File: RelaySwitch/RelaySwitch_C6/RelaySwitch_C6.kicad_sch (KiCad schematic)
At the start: 46 parts, among them J1 AC_MAINS_IN, J3 LOAD_CH1, J4 LOAD_CH2, J5 SW1_INPUT, J6 SW2_INPUT, K1 G5Q-1-DC5, K2 G5Q-1-DC5, Q1 MMBT8050, Q2 MMBT8050, U1 HLK-2M05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

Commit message: relay after layout design
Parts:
- F1: value T250mA/250V -> Littelfuse 443.500; footprint Fuse:Fuseholder_Clip-5x20mm_Littelfuse_111_Inline_P20.00x5.00mm_D1.05mm_Horizontal -> easyeda2kicad:0443500DR; symbol Device:Fuse_Small -> 0443_500:0443.500; Height (none) -> 3.05; Manufacturer_Name (none) -> LITTELFUSE; Manufacturer_Part_Number (none) -> 0443.500
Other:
- moved on the sheet: RV1
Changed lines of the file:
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@@
 	)
 	(junction
+		(at 55.88 25.4)
+		(diameter 0)
+		(color 0 0 0 0)
+	)
+	(junction
 		(at 30.48 163.83)
 		(diameter 0)
@@
 	)
 	(junction
+		(at 49.53 39.37)
+		(diameter 0)
+		(color 0 0 0 0)
+	)
+	(junction
 		(at 90.17 88.9)
 		(diameter 0)
@@
 	)
 	(junction
-		(at 49.53 39.37)
-		(diameter 0)
-		(color 0 0 0 0)
-	)
-	(junction
 		(at 77.47 86.36)
 		(diameter 0)
@@
 	(wire
 		(pts
-			(xy 55.88 36.83) (xy 55.88 40.64)
-		)
-		(stroke
-			(width 0)
-			(type default)
-		)
-	)
-	(wire
-		(pts
 			(xy 30.48 157.48) (xy 30.48 163.83)
 		)
@@
 	(wire
 		(pts
-			(xy 30.48 36.83) (xy 44.45 36.83)
-		)
-		(stroke
-			(width 0)
-			(type default)
-		)
-	)
-	(wire
-		(pts
 			(xy 215.9 102.87) (xy 215.9 105.41)
 		)
@@
 	(wire
 		(pts
-			(xy 55.88 49.53) (xy 55.88 48.26)
-		)
-		(stroke
-			(width 0)
-			(type default)
-		)
-	)
-	(wire
-		(pts
 			(xy 262.89 46.99) (xy 265.43 46.99)
 		)
@@
 	(wire
 		(pts
+			(xy 30.48 36.83) (xy 31.75 36.83)
+		)
+		(stroke
+			(width 0)
+			(type default)
+		)
+	)
+	(wire
+		(pts
 			(xy 156.21 132.08) (xy 156.21 142.24)
 		)
@@
 	(wire
 		(pts
-			(xy 49.53 39.37) (xy 58.42 39.37)
+			(xy 30.48 39.37) (xy 49.53 39.37)
 		)
 		(stroke
@@
 	(wire
 		(pts
+			(xy 55.88 25.4) (xy 55.88 36.83)
+		)
+		(stroke
+			(width 0)
+			(type default)
+		)
+	)
+	(wire
+		(pts
 			(xy 224.79 58.42) (xy 222.25 58.42)
 		)
@@
 	(wire
 		(pts
+			(xy 49.53 25.4) (xy 55.88 25.4)
+		)
+		(stroke
+			(width 0)
+			(type default)
+		)
+	)
+	(wire
+		(pts
 			(xy 106.68 165.1) (xy 125.73 165.1)
 		)
@@
 	(wire
 		(pts
-			(xy 30.48 123.19) (xy 30.48 127)
+			(xy 49.53 39.37) (xy 58.42 39.37)
 		)
 		(stroke
@@
 	(wire
 		(pts
-			(xy 222.25 58.42) (xy 222.25 76.2)
+			(xy 30.48 123.19) (xy 30.48 127)
 		)
 		(stroke
@@
 	(wire
 		(pts
-			(xy 129.54 130.81) (xy 125.73 130.81)
+			(xy 222.25 58.42) (xy 222.25 76.2)
 		)
 		(stroke
@@
 	(wire
 		(pts
-			(xy 262.89 38.1) (xy 267.97 38.1)
+			(xy 129.54 130.81) (xy 125.73 130.81)
 		)
 		(stroke
@@
 	(wire
 		(pts
-			(xy 77.47 63.5) (xy 83.82 63.5)
+			(xy 262.89 38.1) (xy 267.97 38.1)
 		)
 		(stroke
@@
 	(wire
 		(pts
-			(xy 30.48 163.83) (xy 43.18 163.83)
+			(xy 77.47 63.5) (xy 83.82 63.5)
 		)
 		(stroke
@@
 	(wire
 		(pts
-			(xy 49.53 39.37) (xy 49.53 49.53)
+			(xy 30.48 163.83) (xy 43.18 163.83)
 		)
 		(stroke
@@
 	(wire
 		(pts
-			(xy 55.88 36.83) (xy 55.88 25.4)
-		)
-		(stroke
-			(width 0)
-			(type default)
-		)
-	)
-	(wire
-		(pts
 			(xy 68.58 165.1) (xy 106.68 165.1)
 		)
@@
 	(wire
 		(pts
-			(xy 30.48 39.37) (xy 49.53 39.37)
-		)
-		(stroke
-			(width 0)
-			(type default)
-		)
-	)
-	(wire
-		(pts
 			(xy 267.97 38.1) (xy 273.05 38.1)
 		)
@@
 	(wire
 		(pts
-			(xy 49.53 49.53) (xy 55.88 49.53)
-		)
-		(stroke
-			(width 0)
-			(type default)
-		)
-	)
-	(wire
-		(pts
 			(xy 175.26 151.13) (xy 175.26 157.48)
 		)
@@
 	(wire
 		(pts
+			(xy 49.53 34.29) (xy 49.53 39.37)
+		)
+		(stroke
+			(width 0)
+			(type default)
+		)
+	)
+	(wire
+		(pts
 			(xy 30.48 41.91) (xy 44.45 41.91)
 		)
@@
 	(wire
 		(pts
+			(xy 49.53 26.67) (xy 49.53 25.4)
+		)
+		(stroke
+			(width 0)
+			(type default)
+		)
+	)
+	(wire
+		(pts
 			(xy 83.82 60.96) (xy 83.82 63.5)
 		)
@@
 	)
 	(label "L"
-		(at 34.29 36.83 0)
+		(at 30.48 36.83 0)
 		(effects
 			(font
@@
 	(symbol
 		(lib_id "Device:Varistor")
-		(at 55.88 44.45 0)
+		(at 49.53 30.48 0)
 		(unit 1)
 		(exclude_from_sim no)
@@
 		(dnp no)
 		(property "Reference" "RV1"
-			(at 51.054 44.958 0)
+			(at 50.8 29.972 0)
 			(effects
 				(font
@@
 		)
 		(property "Value" "275VAC MOV"
-			(at 56.134 49.276 0)
+			(at 36.83 26.924 0)
 			(effects
 				(font
@@
 		)
 		(property "Footprint" "Varistor:RV_Disc_D7mm_W3.4mm_P5mm"
-			(at 54.102 44.45 90)
+			(at 47.752 30.48 90)
 			(effects
 				(font
@@
 		)
 		(property "Datasheet" "~"
-			(at 55.88 44.45 0)
+			(at 49.53 30.48 0)
 			(effects
 				(font
@@
 		)
 		(property "Description" "Voltage dependent resistor"
-			(at 55.88 44.45 0)
+			(at 49.53 30.48 0)
 			(effects
 				(font
@@
 		)
 		(property "Sim.Name" "kicad_builtin_varistor"
-			(at 55.88 44.45 0)
+			(at 49.53 30.48 0)
 			(effects
 				(font
@@
 		)
 		(property "Sim.Device" "SUBCKT"
-			(at 55.88 44.45 0)
+			(at 49.53 30.48 0)
 			(effects
 				(font
@@
 		)
 		(property "Sim.Pins" "1=A 2=B"
-			(at 55.88 44.45 0)
+			(at 49.53 30.48 0)
 			(effects
 				(font
@@
 		)
 		(property "Sim.Params" "threshold=1k"
-			(at 55.88 44.45 0)
+			(at 49.53 30.48 0)
 			(effects
 				(font
@@
 		)
 		(property "Sim.Library" "${KICAD9_SYMBOL_DIR}/Simulation_SPICE.sp"
-			(at 55.88 44.45 0)
+			(at 49.53 30.48 0)
 			(effects
 				(font
@@
 	)
 	(symbol
-		(lib_id "Device:Fuse_Small")
-		(at 46.99 36.83 0)
+		(lib_id "0443_500:0443.500")
+		(at 31.75 36.83 0)
 		(unit 1)
 		(exclude_from_sim no)
@@
 		(dnp no)
 		(property "Reference" "F1"
-			(at 46.736 34.798 0)
+			(at 40.64 34.544 0)
 			(effects
 				(font
@@
 			)
 		)
-		(property "Value" "T250mA/250V"
-			(at 46.228 31.75 0)
+		(property "Value" "Littelfuse 443.500"
+			(at 36.576 32.766 0)
 			(effects
 				(font
@@
 			)
 		)
-		(property "Footprint" "Fuse:Fuseholder_Clip-5x20mm_Littelfuse_111_Inline_P20.00x5.00mm_D1.05mm_Horizontal"
-			(at 46.99 36.83 0)
+		(property "Footprint" "easyeda2kicad:0443500DR"
+			(at 45.72 133.02 0)
 			(effects
 				(font
 					(size 1.27 1.27)
 				)
+				(justify left top)
 				(hide yes)
 			)
 		)
-		(property "Datasheet" ""
-			(at 46.99 36.83 0)
+		(property "Datasheet" "https://www.littelfuse.com/~/media/electronics/datasheets/fuses/littelfuse_fuse_443_datasheet.pdf.pdf"
+			(at 45.72 233.02 0)
 			(effects
 				(font
 					(size 1.27 1.27)
 				)
+				(justify left top)
 				(hide yes)
 			)
 		)
-		(property "Description" ""
-			(at 46.99 36.83 0)
+		(property "Description" "Surface Mount Fuses 280VAC 0.5A .6ohms 443LC NANO2"
+			(at 31.75 36.83 0)
+			(effects
+				(font
+					(size 1.27 1.27)
+				)
+				(hide yes)
+			)
+		)
+		(property "Height" "3.05"
+			(at 45.72 433.02 0)
+			(effects
+				(font
+					(size 1.27 1.27)
+				)
+				(justify left top)
+				(hide yes)
+			)
+		)
+		(property "Manufacturer_Name" "LITTELFUSE"
+			(at 45.72 533.02 0)
 			(effects
 				(font
 					(size 1.27 1.27)
 				)
+				(justify left top)
+				(hide yes)
+			)
+		)
+		(property "Manufacturer_Part_Number" "0443.500"
+			(at 45.72 633.02 0)
+			(effects
+				(font
+					(size 1.27 1.27)
+				)
+				(justify left top)
+				(hide yes)
+			)
+		)
+		(property "Mouser Part Number" ""
+			(at 45.72 733.02 0)
+			(effects
+				(font
+					(size 1.27 1.27)
+				)
+				(justify left top)
+				(hide yes)
+			)
+		)
+		(property "Mouser Price/Stock" ""
+			(at 45.72 833.02 0)
+			(effects
+				(font
+					(size 1.27 1.27)
+				)
+				(justify left top)
+				(hide yes)
+			)
+		)
+		(property "Arrow Part Number" ""
+			(at 45.72 933.02 0)
+			(effects
+				(font
+					(size 1.27 1.27)
+				)
+				(justify left top)
+				(hide yes)
+			)
+		)
+		(property "Arrow Price/Stock" ""
+			(at 45.72 1033.02 0)
+			(effects
+				(font
+					(size 1.27 1.27)
+				)
+				(justify left top)
 				(hide yes)
 			)

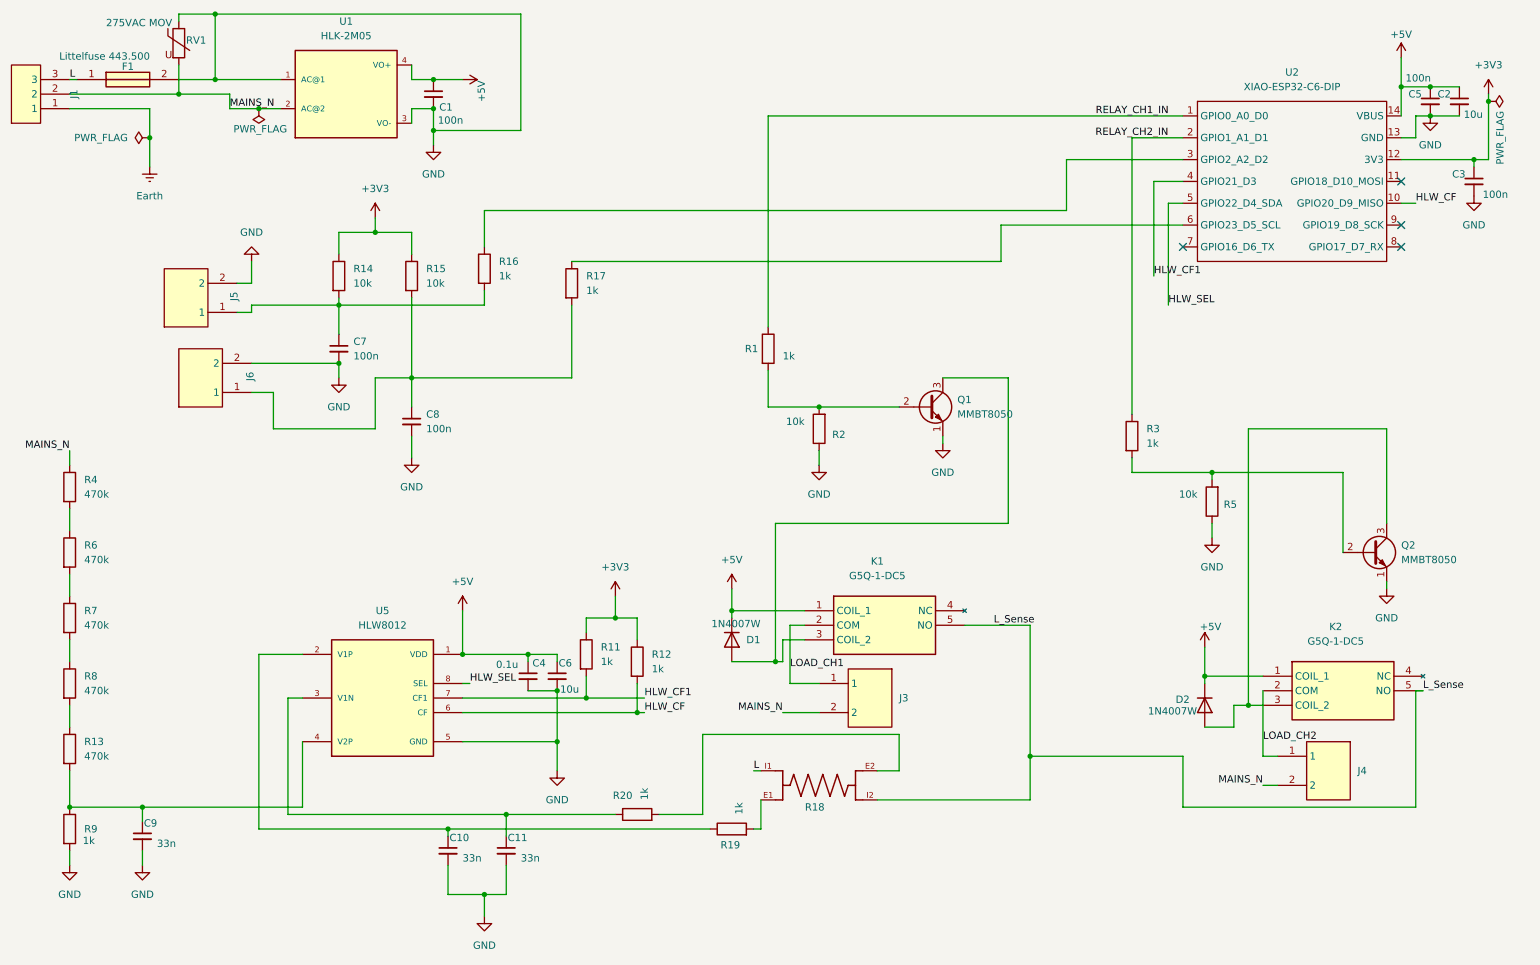
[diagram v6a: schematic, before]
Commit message: replaced the Q1 and 2 with Dual driver
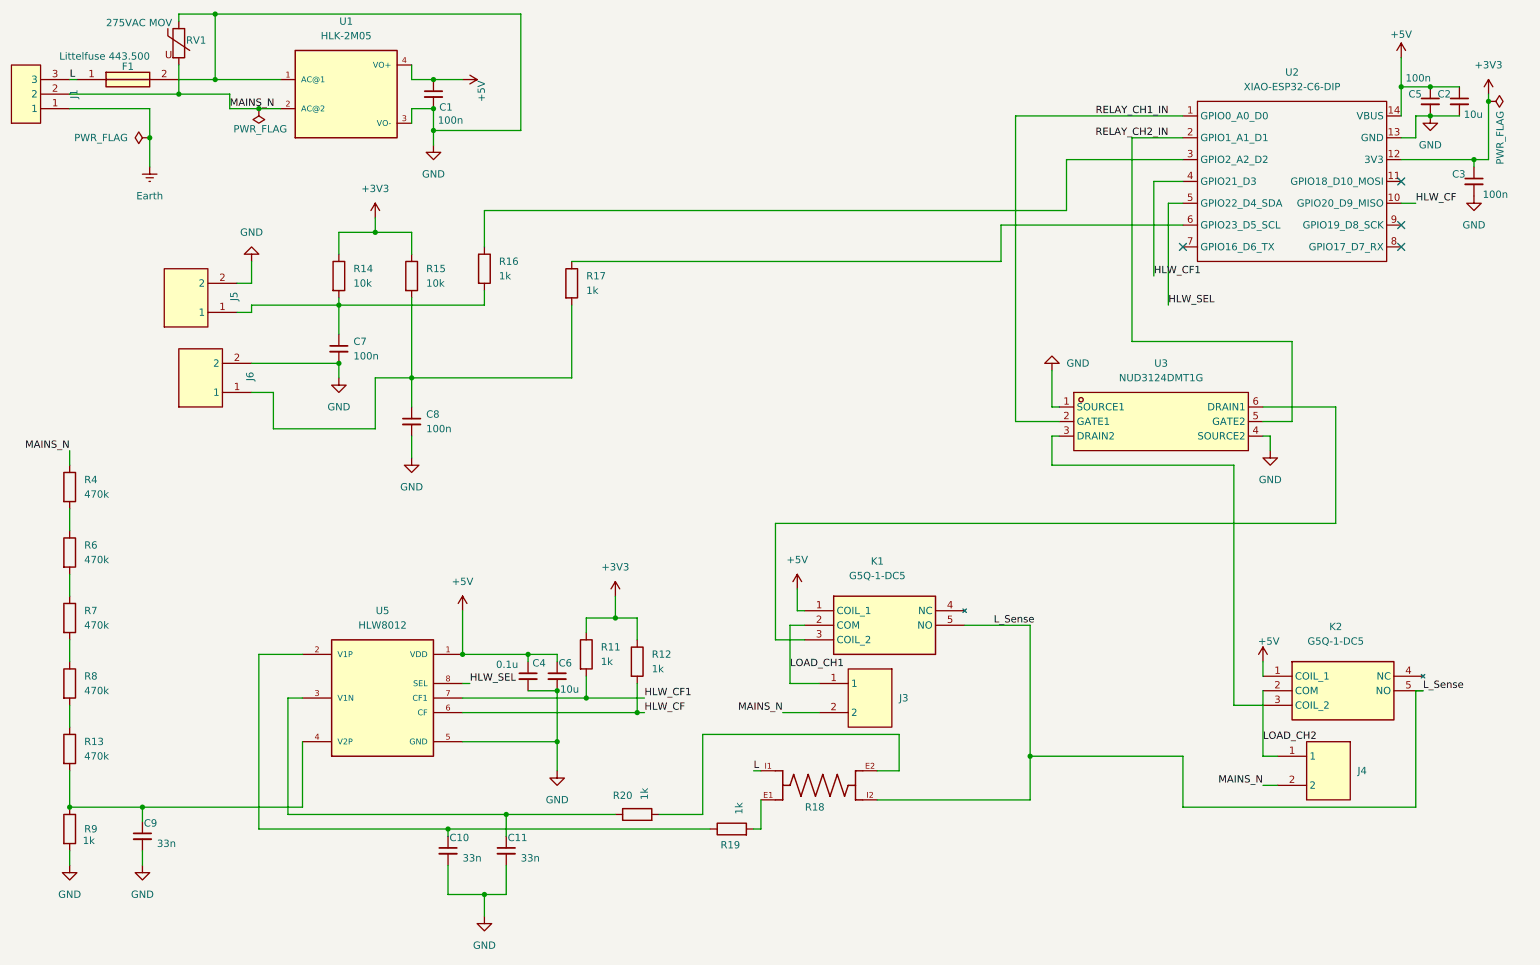
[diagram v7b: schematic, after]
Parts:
- removed D1, D2: 1N4007W, Diode_SMD:D_SMA, symbol Diode:1N4007
- removed Q2: MMBT8050, Package_TO_SOT_SMD:SOT-23, symbol Transistor_BJT:S8050
- removed R1, R3: 1k, Resistor_SMD:R_0603_1608Metric, symbol Device:R
- removed R2, R5: 10k, Resistor_SMD:R_0402_1005Metric, symbol Device:R
- U3: renamed from Q1; value MMBT8050 -> NUD3124DMT1G; footprint Package_TO_SOT_SMD:SOT-23 -> easyeda2kicad:SC-74-6_L3.0-W1.5-P0.95-LS2.8-BL; symbol Transistor_BJT:S8050 -> NUD3124DMT1G:NUD3124DMT1G; LCSC Part (none) -> C182473
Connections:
- net GND: now also U3.4 (SOURCE2)
- net RELAY_CH1_IN: now also U3.2 (GATE1)
- net RELAY_CH2_IN: now also U3.5 (GATE2)
- net at U3.3 (DRAIN2): now also K2.3 (COIL_2); no longer K1.3 (COIL_2)
- new net: K1.3 (COIL_2), U3.6 (DRAIN1)
